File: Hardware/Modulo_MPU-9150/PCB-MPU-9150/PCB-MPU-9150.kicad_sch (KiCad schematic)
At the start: 17 parts, among them P1 CONN_01X08, U1 MPU-9150, U2 AP2112K-3.3

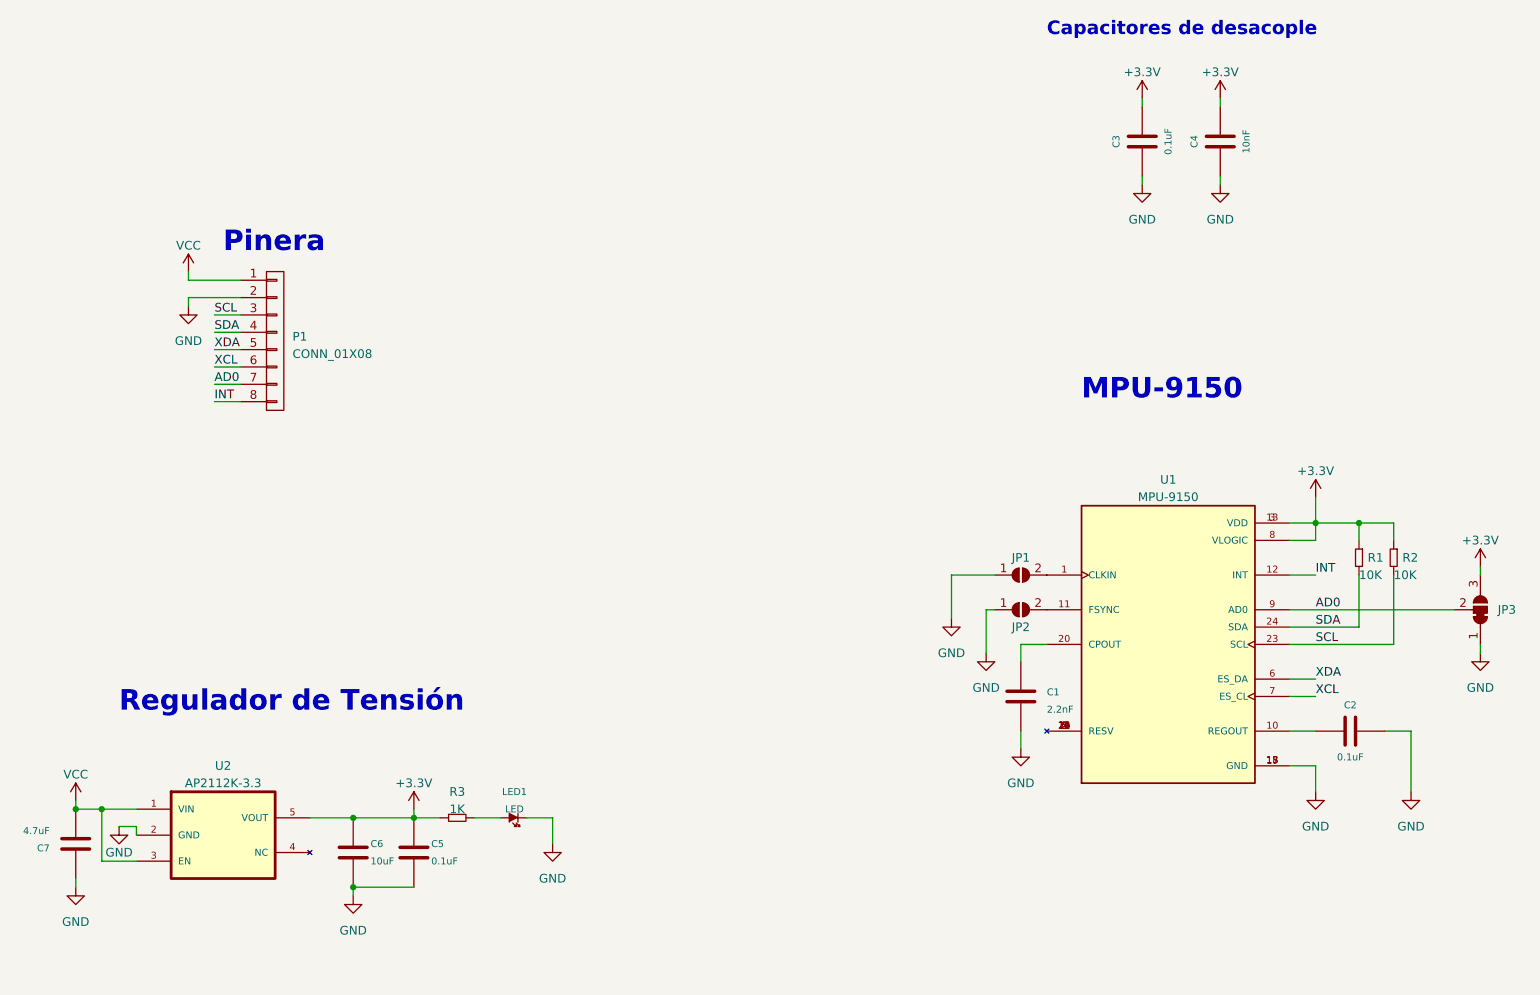
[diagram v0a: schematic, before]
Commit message: agregue la version final de la mpu9150 y la version final del Pla version 2 del PCB
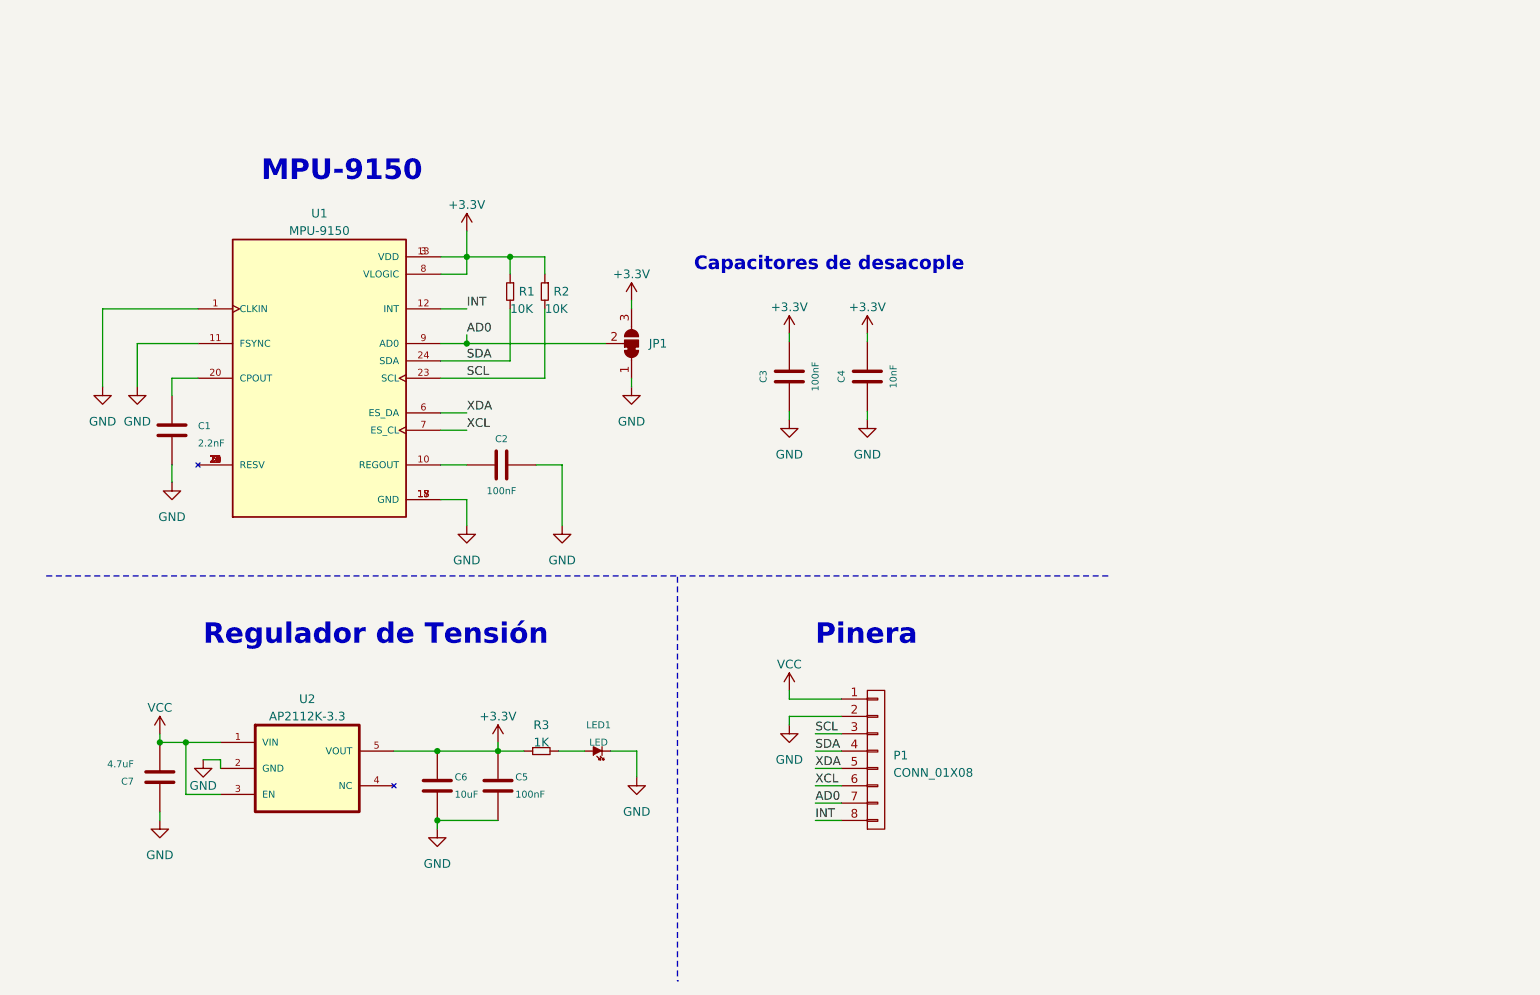
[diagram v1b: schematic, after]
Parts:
- removed JP1, JP2: Jump, symbol Jumper:SolderJumper_2_Open
- removed JP3: Jump, symbol Jumper:SolderJumper_3_Bridged12
- added JP1: Jump, EESTN5:R_0805, symbol Jumper:SolderJumper_3_Bridged12
- C1, C4, C6, C7: footprint (none) -> footprints:C_0603
- C2, C3, C5: value 0.1uF -> 100nF; footprint (none) -> footprints:C_0603
- LED1: footprint (none) -> EESTN5:Led_0805
- P1: footprint (none) -> footprints:GY-521-MPU-6050
- R1, R2, R3: footprint (none) -> EESTN5:R_0805
- U1: footprint PQFN50P400X400X110-24N -> footprints:MPU-9150-Qfn-24
- U2: footprint (none) -> footprints:AP2112K-3.3-Sot25
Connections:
- net +3.3V: now also JP1.3 (B)
- net AD0: now also JP1.2 (C)
- net GND: now also U1.1 (CLKIN), U1.11 (FSYNC), JP1.1 (A)
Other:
- company: (none) -> Bover GROUP
- moved on the sheet: C1, C2, C3, C4, C5, C6, C7, LED1, P1, R1, R2, R3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
